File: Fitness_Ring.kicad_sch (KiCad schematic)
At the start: 30 parts, among them U1 NRF52832-QFAA-R, U2 MAX30102, U3 MIC5370-SGYMT-TR, U4 MCP73831-2-OT, U6 MAX30205MTA_, Y1 32.768kHz

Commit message: changed the board to a flex board, added keepout zones and ground pour for bottom layer, need to fix Antenna
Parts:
- C1, C10, C11, C13, C2, C3, C4, C5, C6, C7, C8, C9: footprint Capacitor_SMD:C_0402_1005Metric -> Capacitor_SMD:C_0201_0603Metric
- D1: footprint LED_SMD:LED_0603_1608Metric -> LED_SMD:LED_0201_0603Metric
- L1: footprint Inductor_SMD:L_0402_1005Metric -> Inductor_SMD:L_0201_0603Metric
- R1, R2, R3, R4, R5, R6, R7, R8: footprint Resistor_SMD:R_0402_1005Metric -> Resistor_SMD:R_0201_0603Metric
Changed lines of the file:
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@@
 		)
 	)
+	(label "ANT"
+		(at 129.54 48.26 0)
+		(effects
+			(font
+				(size 1.27 1.27)
+			)
+			(justify left bottom)
+		)
+	)
 	(label "SCL"
 		(at 35.56 86.36 180)
@@
 		)
 	)
-	(label "GND_RF"
-		(at 127 55.88 270)
-		(effects
-			(font
-				(size 1.27 1.27)
-			)
-			(justify right bottom)
-		)
-	)
 	(label "SDA"
 		(at 198.12 48.26 180)
@@
 		)
 	)
-	(label "ANT"
-		(at 129.54 48.26 0)
-		(effects
-			(font
-				(size 1.27 1.27)
-			)
-			(justify left bottom)
-		)
-	)
 	(symbol
 		(lib_id "power:+3.3V")
@@
 			)
 		)
-		(property "Footprint" "Capacitor_SMD:C_0402_1005Metric"
+		(property "Footprint" "Capacitor_SMD:C_0201_0603Metric"
 			(at 270.51 134.3152 0)
 			(effects
@@
 			)
 		)
-		(property "Footprint" "Inductor_SMD:L_0402_1005Metric"
+		(property "Footprint" "Inductor_SMD:L_0201_0603Metric"
 			(at 121.92 48.26 0)
 			(effects
@@
 	(symbol
 		(lib_id "power:GND")
+		(at 127 55.88 0)
+		(unit 1)
+		(exclude_from_sim no)
+		(in_bom yes)
+		(on_board yes)
+		(dnp no)
+		(fields_autoplaced yes)
+		(property "Reference" "#PWR05"
+			(at 127 62.23 0)
+			(effects
+				(font
+					(size 1.27 1.27)
+				)
+				(hide yes)
+			)
+		)
+		(property "Value" "GND"
+			(at 127 60.96 0)
+			(effects
+				(font
+					(size 1.27 1.27)
+				)
+			)
+		)
+		(property "Footprint" ""
+			(at 127 55.88 0)
+			(effects
+				(font
+					(size 1.27 1.27)
+				)
+				(hide yes)
+			)
+		)
+		(property "Datasheet" ""
+			(at 127 55.88 0)
+			(effects
+				(font
+					(size 1.27 1.27)
+				)
+				(hide yes)
+			)
+		)
+		(property "Description" "Power symbol creates a global label with name \"GND\" , ground"
+			(at 127 55.88 0)
+			(effects
+				(font
+					(size 1.27 1.27)
+				)
+				(hide yes)
+			)
+		)
+		(pin "1"
+		)
+		(instances
+			(project "Fitness_Ring"
+				(path "/909198cc-2369-401c-be36-c86b01c4a982"
+					(reference "#PWR05")
+					(unit 1)
+				)
+			)
+		)
+	)
+	(symbol
+		(lib_id "power:GND")
 		(at 207.01 110.49 0)
 		(unit 1)
@@
 			)
 		)
-		(property "Footprint" "Resistor_SMD:R_0402_1005Metric"
+		(property "Footprint" "Resistor_SMD:R_0201_0603Metric"
 			(at 174.752 152.4 90)
 			(effects
@@
 			)
 		)
-		(property "Footprint" "Capacitor_SMD:C_0402_1005Metric"
+		(property "Footprint" "Capacitor_SMD:C_0201_0603Metric"
 			(at 171.7548 135.89 0)
 			(effects
@@
 			)
 		)
-		(property "Footprint" "Capacitor_SMD:C_0402_1005Metric"
+		(property "Footprint" "Capacitor_SMD:C_0201_0603Metric"
 			(at 20.0152 148.59 0)
 			(effects
@@
 			)
 		)
-		(property "Footprint" "Capacitor_SMD:C_0402_1005Metric"
+		(property "Footprint" "Capacitor_SMD:C_0201_0603Metric"
 			(at 138.43 39.6748 0)
 			(effects
@@
 			)
 		)
-		(property "Footprint" "Capacitor_SMD:C_0402_1005Metric"
+		(property "Footprint" "Capacitor_SMD:C_0201_0603Metric"
 			(at 126.0348 48.26 0)
 			(effects
@@
 			)
 		)
-		(property "Footprint" "Capacitor_SMD:C_0402_1005Metric"
+		(property "Footprint" "Capacitor_SMD:C_0201_0603Metric"
 			(at 20.32 41.6052 0)
 			(effects
@@
 			)
 		)
-		(property "Footprint" "Resistor_SMD:R_0402_1005Metric"
+		(property "Footprint" "Resistor_SMD:R_0201_0603Metric"
 			(at 207.01 147.828 90)
 			(effects
@@
 			)
 		)
-		(property "Footprint" "Resistor_SMD:R_0402_1005Metric"
+		(property "Footprint" "Resistor_SMD:R_0201_0603Metric"
 			(at 264.922 142.24 90)
 			(effects
@@
 			)
 		)
-		(property "Footprint" "Resistor_SMD:R_0402_1005Metric"
+		(property "Footprint" "Resistor_SMD:R_0201_0603Metric"
 			(at 127.762 67.31 90)
 			(effects
@@
 			)
 		)
-		(property "Footprint" "Resistor_SMD:R_0402_1005Metric"
+		(property "Footprint" "Resistor_SMD:R_0201_0603Metric"
 			(at 229.362 87.63 90)
 			(effects
@@
 			)
 		)
-		(property "Footprint" "Capacitor_SMD:C_0402_1005Metric"
+		(property "Footprint" "Capacitor_SMD:C_0201_0603Metric"
 			(at 219.4052 86.36 0)
 			(effects
@@
 			)
 		)
-		(property "Footprint" "Capacitor_SMD:C_0402_1005Metric"
+		(property "Footprint" "Capacitor_SMD:C_0201_0603Metric"
 			(at 20.32 49.2252 0)
 			(effects
@@
 			)
 		)
-		(property "Footprint" "Resistor_SMD:R_0402_1005Metric"
+		(property "Footprint" "Resistor_SMD:R_0201_0603Metric"
 			(at 136.652 67.31 90)
 			(effects
@@
 			)
 		)
-		(property "Footprint" "Capacitor_SMD:C_0402_1005Metric"
+		(property "Footprint" "Capacitor_SMD:C_0201_0603Metric"
 			(at 129.54 26.9748 0)
 			(effects
@@
 			)
 		)
-		(property "Footprint" "LED_SMD:LED_0603_1608Metric"
+		(property "Footprint" "LED_SMD:LED_0201_0603Metric"
 			(at 210.82 137.16 0)
 			(effects
@@
 			)
 		)
-		(property "Footprint" "Resistor_SMD:R_0402_1005Metric"
+		(property "Footprint" "Resistor_SMD:R_0201_0603Metric"
 			(at 45.212 77.47 90)
 			(effects
@@
 			)
 		)
-		(property "Footprint" "Capacitor_SMD:C_0402_1005Metric"
+		(property "Footprint" "Capacitor_SMD:C_0201_0603Metric"
 			(at 112.7252 156.21 0)
 			(effects
@@
 			)
 		)
-		(property "Footprint" "Capacitor_SMD:C_0402_1005Metric"
+		(property "Footprint" "Capacitor_SMD:C_0201_0603Metric"
 			(at 100.0252 156.21 0)
 			(effects
@@
 			)
 		)
-		(property "Footprint" "Resistor_SMD:R_0402_1005Metric"
+		(property "Footprint" "Resistor_SMD:R_0201_0603Metric"
 			(at 36.322 77.47 90)
 			(effects
@@
 			)
 		)
-		(property "Footprint" "Capacitor_SMD:C_0402_1005Metric"
+		(property "Footprint" "Capacitor_SMD:C_0201_0603Metric"
 			(at 148.59 32.0548 0)
 			(effects

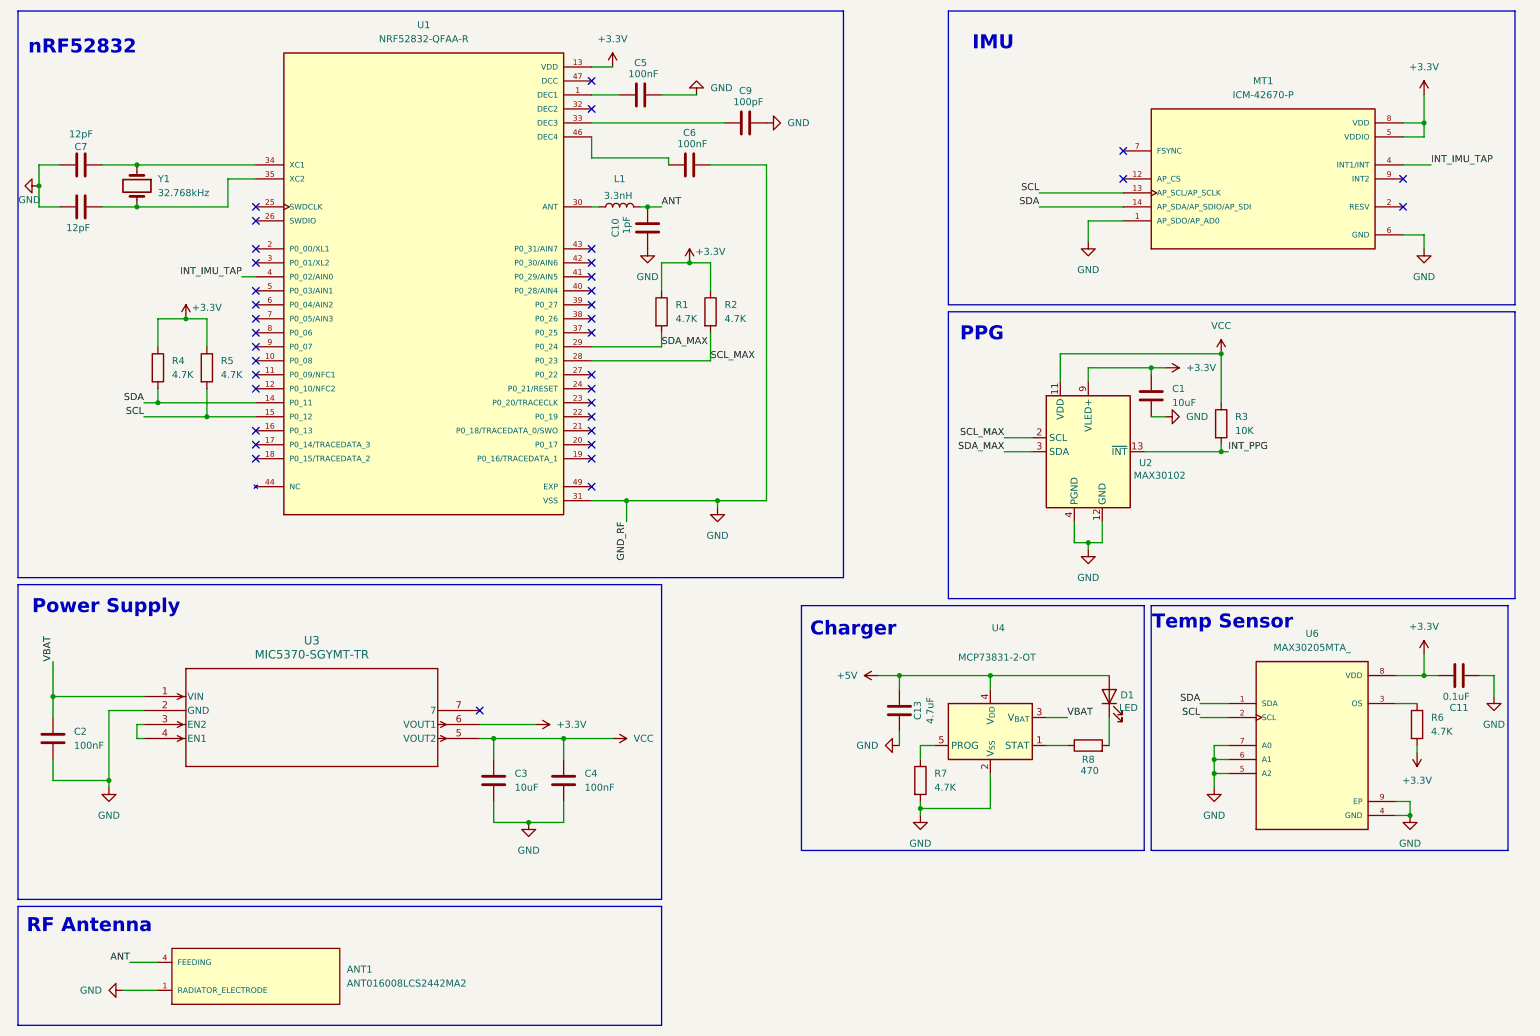
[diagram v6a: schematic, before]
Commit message: Fixed RF pi network and began doing traces
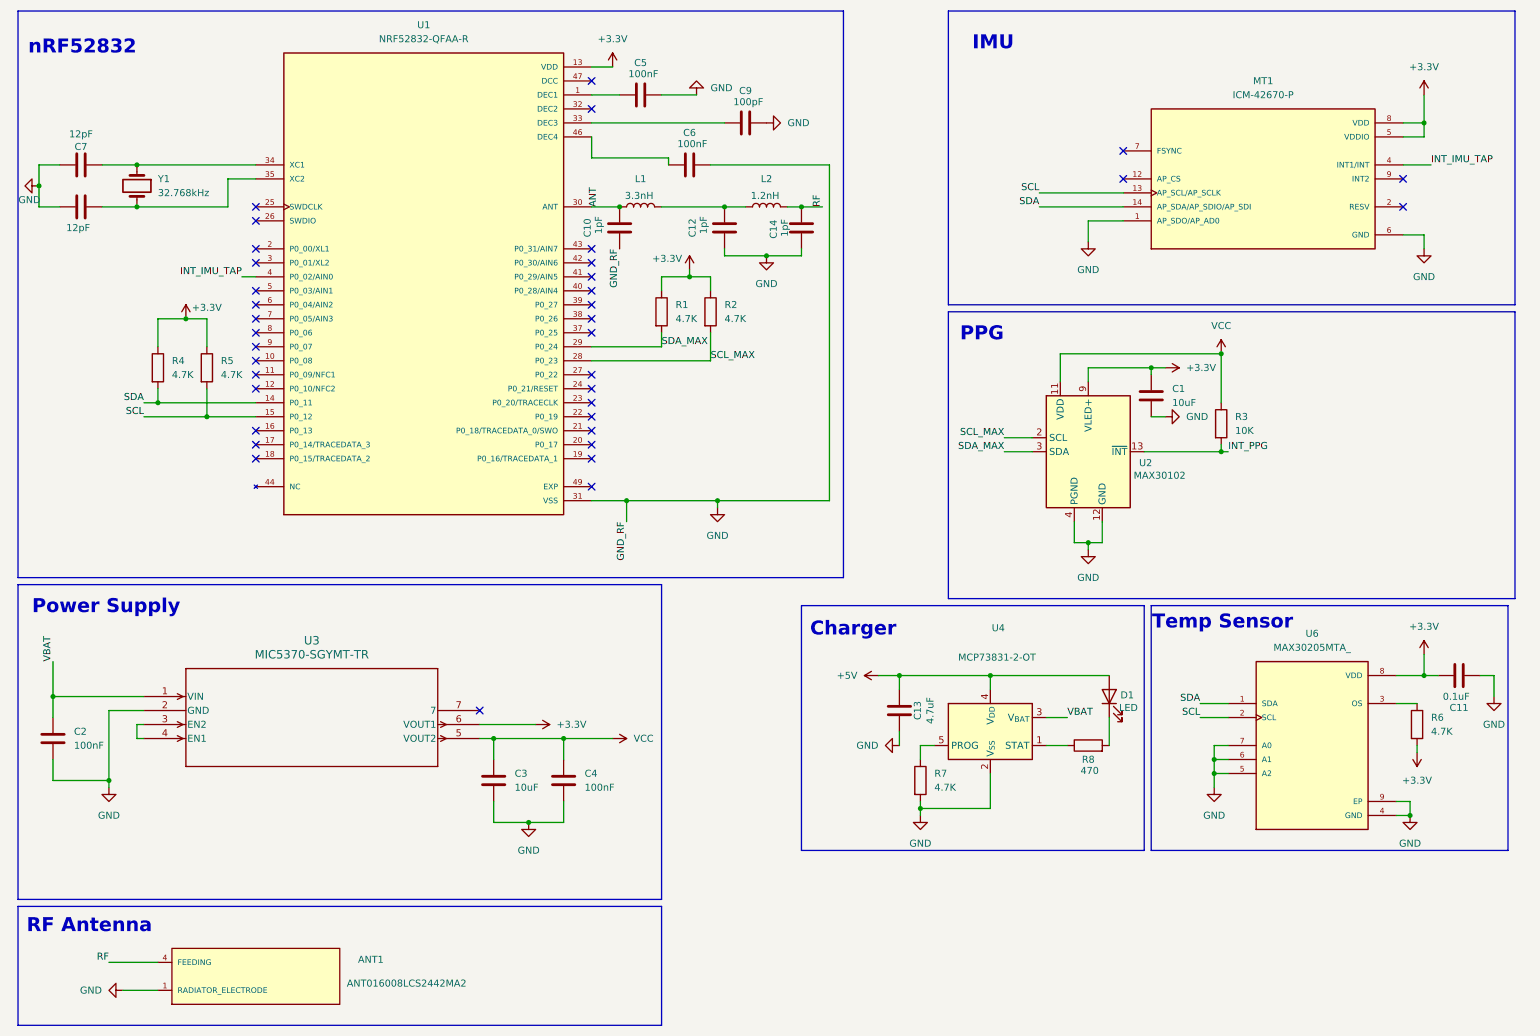
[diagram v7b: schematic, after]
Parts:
- added C12, C14: 1pF, Capacitor_SMD:C_0201_0603Metric, symbol Device:C
- added L2: 1.2nH, Inductor_SMD:L_0201_0603Metric, symbol Device:L
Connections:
- net ANT: now also L1.1, U1.30 (ANT); no longer ANT1.4 (FEEDING), L1.2
- net GND: now also C12.1, C14.1
- new net: C12.2, L1.2, L2.1
- new net RF: ANT1.4 (FEEDING), C14.2, L2.2
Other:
- moved on the sheet: C10, L1
